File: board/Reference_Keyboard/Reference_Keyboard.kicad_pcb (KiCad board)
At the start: 2 copper layers, 157 x 105 mm, 79 parts, among them J1 Conn_01x03_Pin, J2 USB_C_Receptacle_USB2.0, J3 Conn_01x04_Pin, J4 84953-4, SW1 SW_Push, SW10 SW_Push, SW11 SW_Push, SW12 SW_Push, SW13 SW_Push, SW14 SW_Push, SW15 SW_Push, SW16 SW_Push, SW17 SW_Push, SW18 SW_Push, SW19 SW_Push, SW2 SW_Push, SW20 SW_Push, SW21 SW_Push, SW22 SKQGAFE010, SW23 SKQGAFE010, SW24 RotaryEncoder_Switch, SW3 SW_Push, SW4 SW_Push, SW5 SW_Push, SW6 SW_Push, SW7 SW_Push, SW8 SW_Push, SW9 SW_Push, U1 RP2040, U2 W25Q16JVSSIM, U3 LM1117RS-3.3, Y1 NX3225SA-12MHz-STD-CSR-6

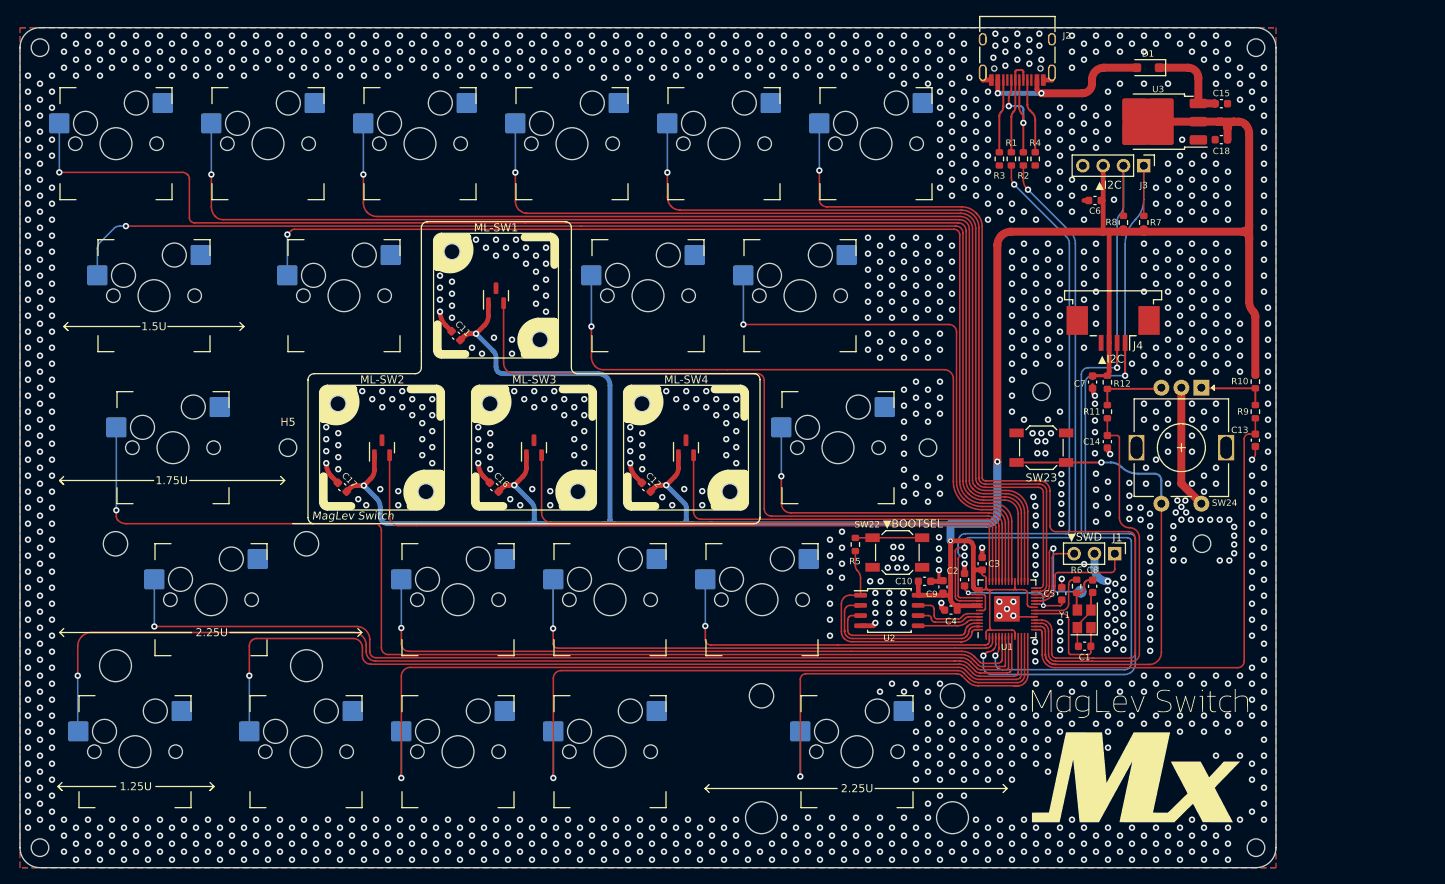
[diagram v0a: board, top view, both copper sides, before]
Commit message: add firmware and PCB for hardware v1.01
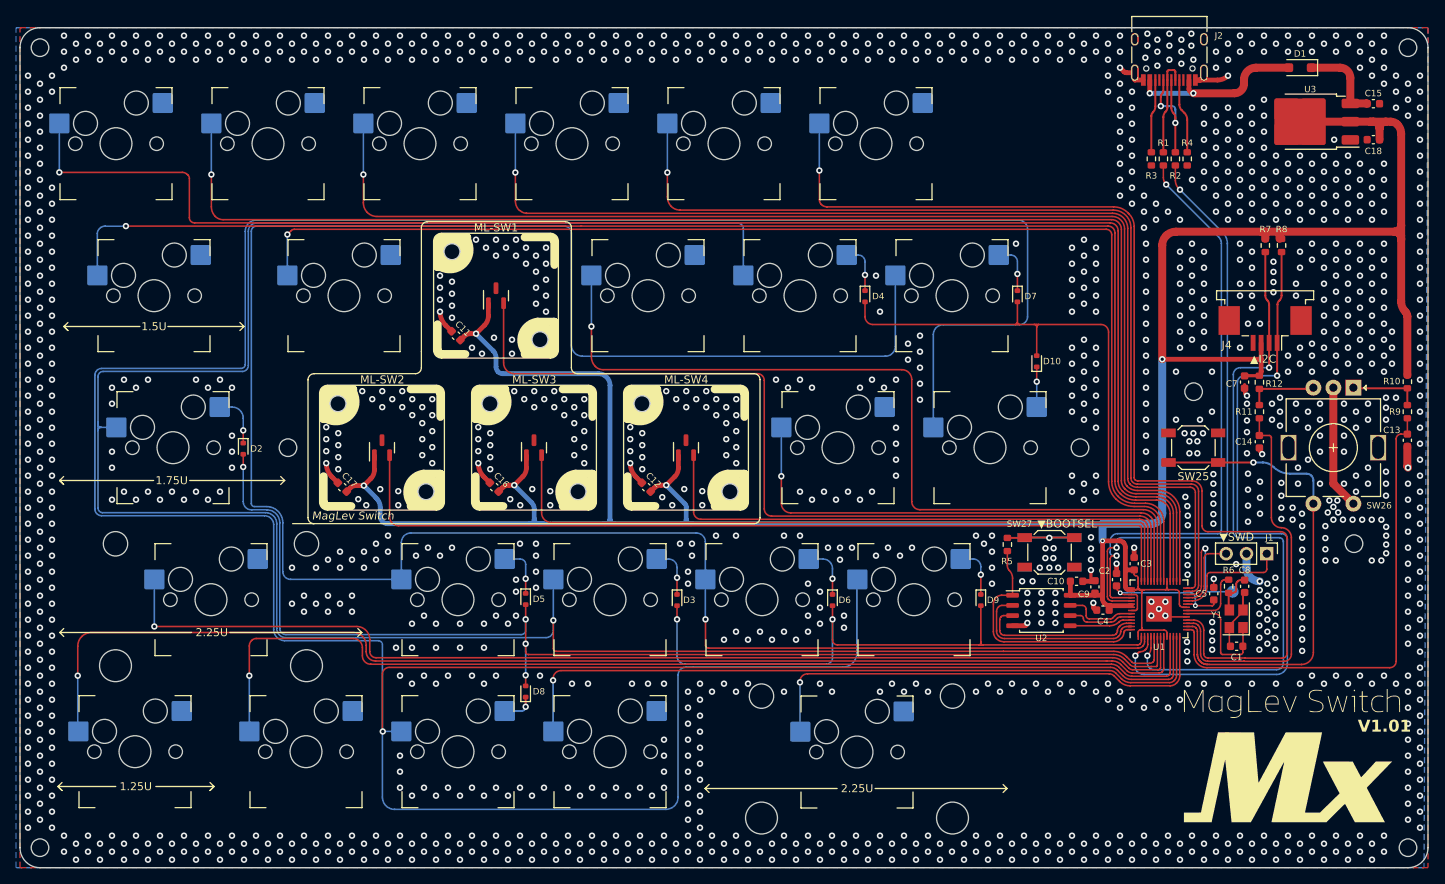
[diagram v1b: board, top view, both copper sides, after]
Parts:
- removed C6: 0.1u, Capacitor_SMD:C_0603_1608Metric
- removed J3: Conn_01x04_Pin, Connector_PinHeader_2.54mm:PinHeader_1x04_P2.54mm_Vertical
- added D10: 1SS387, Diode_SMD:D_SOD-523, F.Cu at (204.1, 92.2)
- added D2: 1SS387, Diode_SMD:D_SOD-523, F.Cu at (104.9, 103.1)
- added D3: 1SS387, Diode_SMD:D_SOD-523, F.Cu at (159.1, 122.0)
- added D4: 1SS387, Diode_SMD:D_SOD-523, F.Cu at (182.6, 84.1)
- added D5: 1SS387, Diode_SMD:D_SOD-523, F.Cu at (140.2, 121.9)
- added D6: 1SS387, Diode_SMD:D_SOD-523, F.Cu at (178.6, 122.0)
- added D7: 1SS387, Diode_SMD:D_SOD-523, F.Cu at (201.7, 84.1)
- added D8: 1SS387, Diode_SMD:D_SOD-523, F.Cu at (140.2, 133.5)
- added D9: 1SS387, Diode_SMD:D_SOD-523, F.Cu at (197.1, 122.0)
- added SW23: SW_Push, MX_Hotswap:MX-Hotswap-1U, F.Cu at (150.8, 141.0)
- added SW26: RotaryEncoder_Switch, Rotary_Encoder:RotaryEncoder_Alps_EC11E-Switch_Vertical_H20mm, F.Cu at (243.7, 95.5)
- added SW27: SKQGAFE010, Button_Switch_SMD:SW_SPST_SKQG_WithStem, F.Cu at (205.7, 116.1)
- added SW28: SKQGAFE010, Button_Switch_SMD:SW_SPST_SKQG_WithStem, B.Cu at (205.7, 116.1)
- SW11: footprint MX_Hotswap:MX-Hotswap-1.75U -> MX_Hotswap:MX-Hotswap-1U
- SW12: footprint MX_Hotswap:MX-Hotswap-1U -> MX_Hotswap:MX-Hotswap-1.75U
- SW13, SW21: footprint MX_Hotswap:MX-Hotswap-2.25U -> MX_Hotswap:MX-Hotswap-1U
- SW15: footprint MX_Hotswap:MX-Hotswap-1U -> MX_Hotswap:MX-Hotswap-2.25U
- SW17: footprint MX_Hotswap:MX-Hotswap-1.25U -> MX_Hotswap:MX-Hotswap-1U
- SW20: footprint MX_Hotswap:MX-Hotswap-1U -> MX_Hotswap:MX-Hotswap-1.25U
- SW22: value SKQGAFE010 -> SW_Push; footprint Button_Switch_SMD:SW_SPST_SKQG_WithStem -> MX_Hotswap:MX-Hotswap-1U
- SW24: renamed from SW23; value SKQGAFE010 -> SW_Push; footprint Button_Switch_SMD:SW_SPST_SKQG_WithStem -> MX_Hotswap:MX-Hotswap-2.25U
- SW25: renamed from SW24; value RotaryEncoder_Switch -> SKQGAFE010; footprint Rotary_Encoder:RotaryEncoder_Alps_EC11E-Switch_Vertical_H20mm -> Button_Switch_SMD:SW_SPST_SKQG_WithStem
- moved SW11 99.2 mm to (193.5, 84.0)
- moved SW12 83.1 mm to (96.1, 103.0)
- moved SW13 80.6 mm to (179.2, 103.0)
- moved SW14 69.2 mm to (198.2, 103.0)
- moved SW21 68.9 mm to (112.8, 141.0)
- moved SW17 62.3 mm to (150.8, 122.0)
- moved SW22 60.3 mm to (131.8, 141.0), turned to 0 degrees
- moved SW18 60.1 mm to (169.8, 122.0)
- moved SW19 60.1 mm to (188.8, 122.0)
- moved SW20 59.4 mm to (91.4, 141.0)
- moved SW15 49.9 mm to (100.9, 122.0)
- moved SW24 44.5 mm to (181.6, 141.0), turned to 0 degrees
- moved SW16 38.0 mm to (131.8, 122.0)
- moved C1 19.0 mm to (229.1, 127.8)
- moved C10 19.0 mm to (209.1, 119.7)
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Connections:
- SW10 pad 1: /R -> /ROW1
- SW10 pad 2: GND -> Net-(D4-K)
- SW11 pad 1: /CAPS -> /ROW2
- SW11 pad 2: GND -> Net-(D7-K)
- SW12 pad 1: /F -> /ROW1
- SW12 pad 2: GND -> Net-(D2-K)
- SW13 pad 1: /SHIFT -> /F
- SW14 pad 1: /Z -> /ROW3
- SW14 pad 2: GND -> Net-(D10-K)
- SW15 pad 1: /X -> /SHIFT
- SW16 pad 1: /C -> /ROW2
- SW16 pad 2: GND -> Net-(D5-K)
- SW17 pad 1: /CTRL -> /ROW1
- SW17 pad 2: GND -> Net-(D3-K)
- SW18 pad 1: /Fn -> /ROW2
- SW18 pad 2: GND -> Net-(D6-K)
- SW19 pad 1: /SUPER -> /ROW3
- SW19 pad 2: GND -> Net-(D9-K)
- SW20 pad 1: /ALT -> /CTRL
- SW21 pad 1: /SPACE -> /Fn
- SW22 pad 1: GND -> /ROW3
- SW22 pad 2: Net-(R5-Pad2) -> Net-(D8-K)
- SW24 pad 1: /BUTTON1 -> /SPACE
- U1 pad 12: /SUPER -> /ROW3
- U1 pad 2: /C -> /COL2
- U1 pad 3: /X -> /ROW2
- U1 pad 35: /R -> /COL3
- U1 pad 6: /Z -> /ROW1
- U1 pad 7: /CAPS -> /COL1
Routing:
- net /ROW3: track 0.00 -> 458.9 mm, vias 0 -> 1
- net /ROW1: track 0.00 -> 285.6 mm, vias 0 -> 1
- net /ROW2: track 0.00 -> 279.1 mm, vias 0 -> 1
- net /COL1: track 0.00 -> 152.4 mm, vias 0 -> 4
- net /CAPS: track 142.5 -> 0.00 mm, vias 1 -> 0
- net /SUPER: track 101.8 -> 0.00 mm, vias 1 -> 0
- net /Z: track 87.3 -> 0.00 mm, vias 1 -> 0
- net /COL2: track 0.00 -> 81.4 mm, vias 0 -> 2
- net /COL3: track 0.00 -> 76.7 mm
- net /R: track 68.6 -> 0.00 mm, vias 1 -> 0
- net /X: track 64.4 -> 0.00 mm, vias 1 -> 0
- net /C: track 44.2 -> 0.00 mm, vias 1 -> 0
- net /SDA: track 108.4 -> 86.8 mm
- net /SCL: track 102.9 -> 82.6 mm
- net /E: track 86.4 -> 106.4 mm
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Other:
- board size 157 x 105 mm -> 176 x 105 mm
- board text added: "V1.01"
